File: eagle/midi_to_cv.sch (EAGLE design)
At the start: 58 parts, among them IC1 TL084P, IC2 TL084P, U1 ATMEGA328P_PDIP

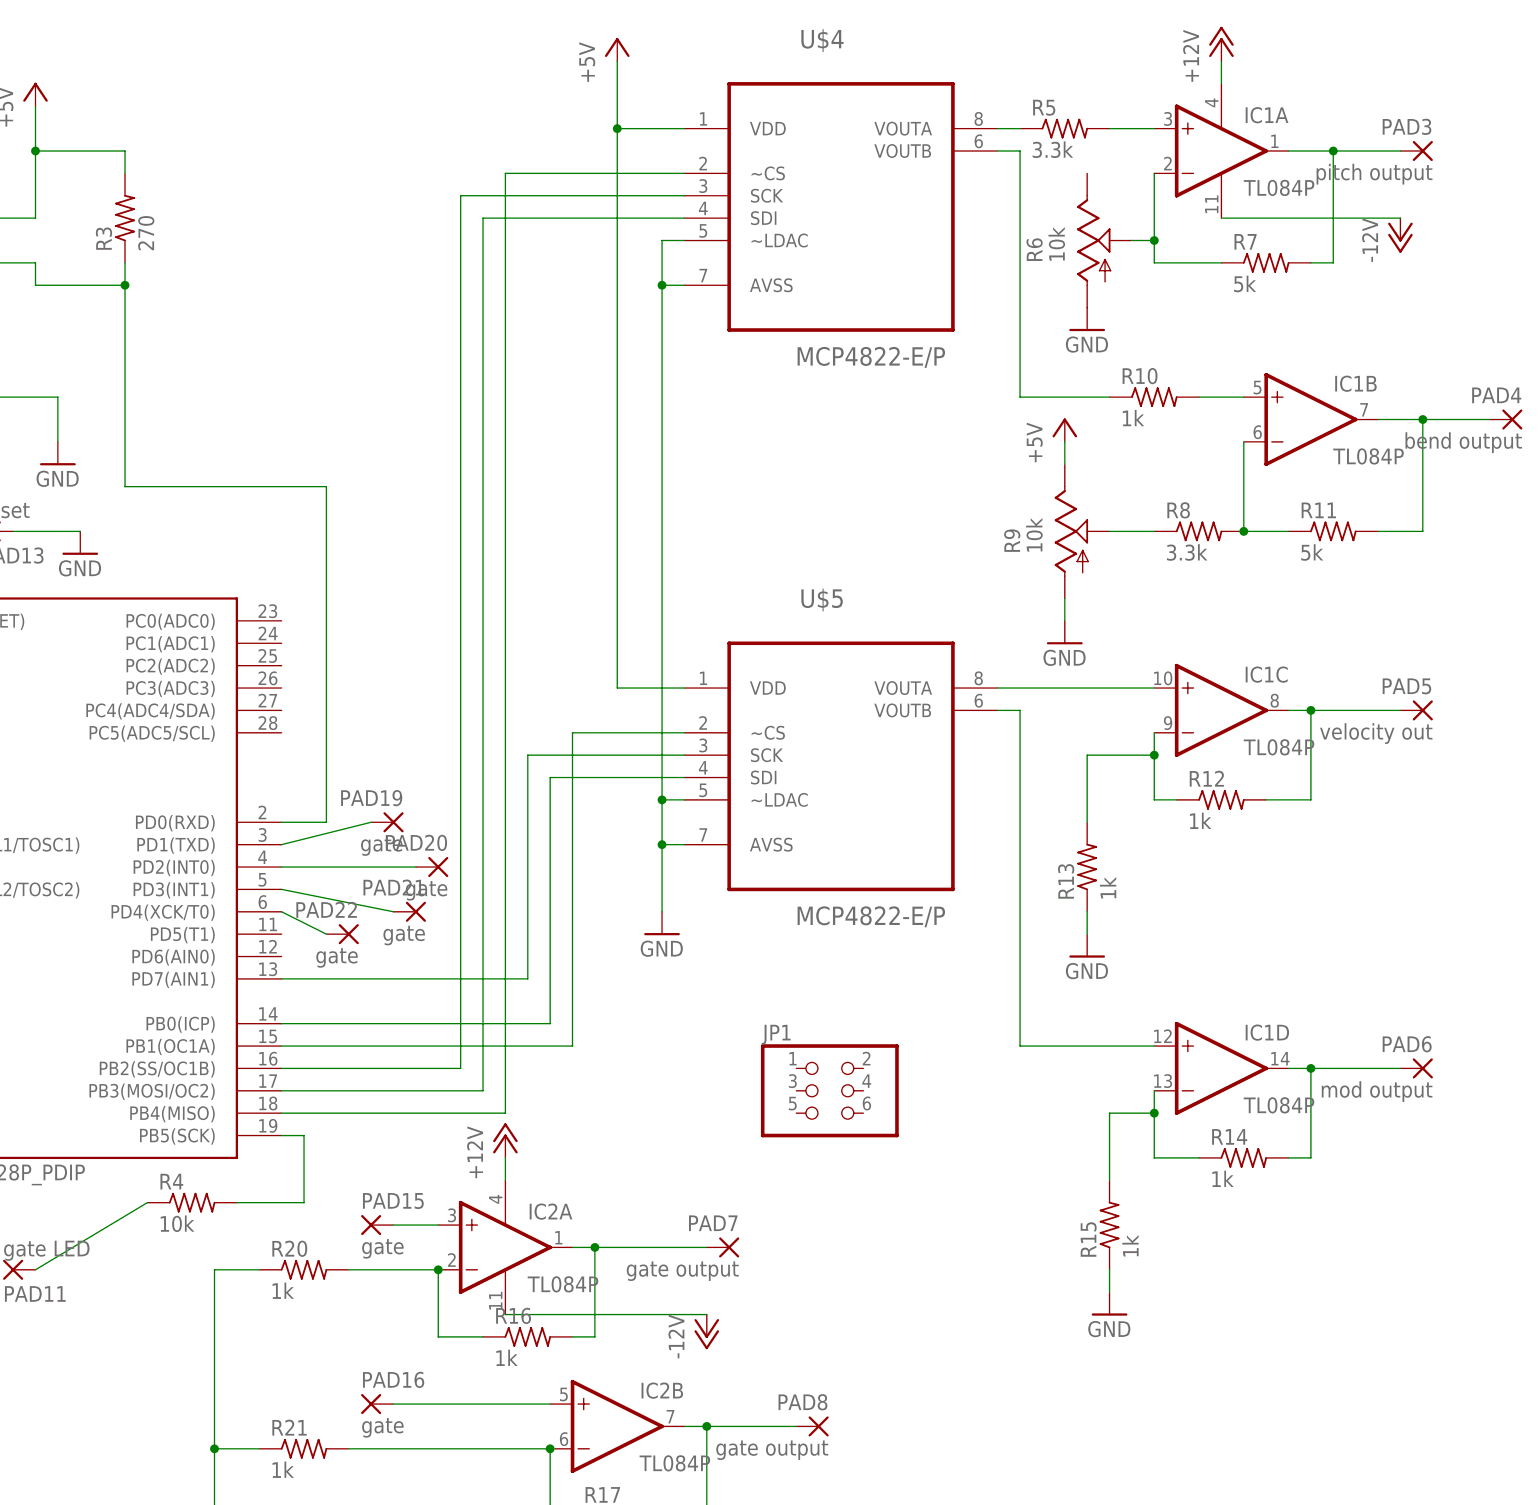
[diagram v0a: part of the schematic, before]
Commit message: converting to poly4
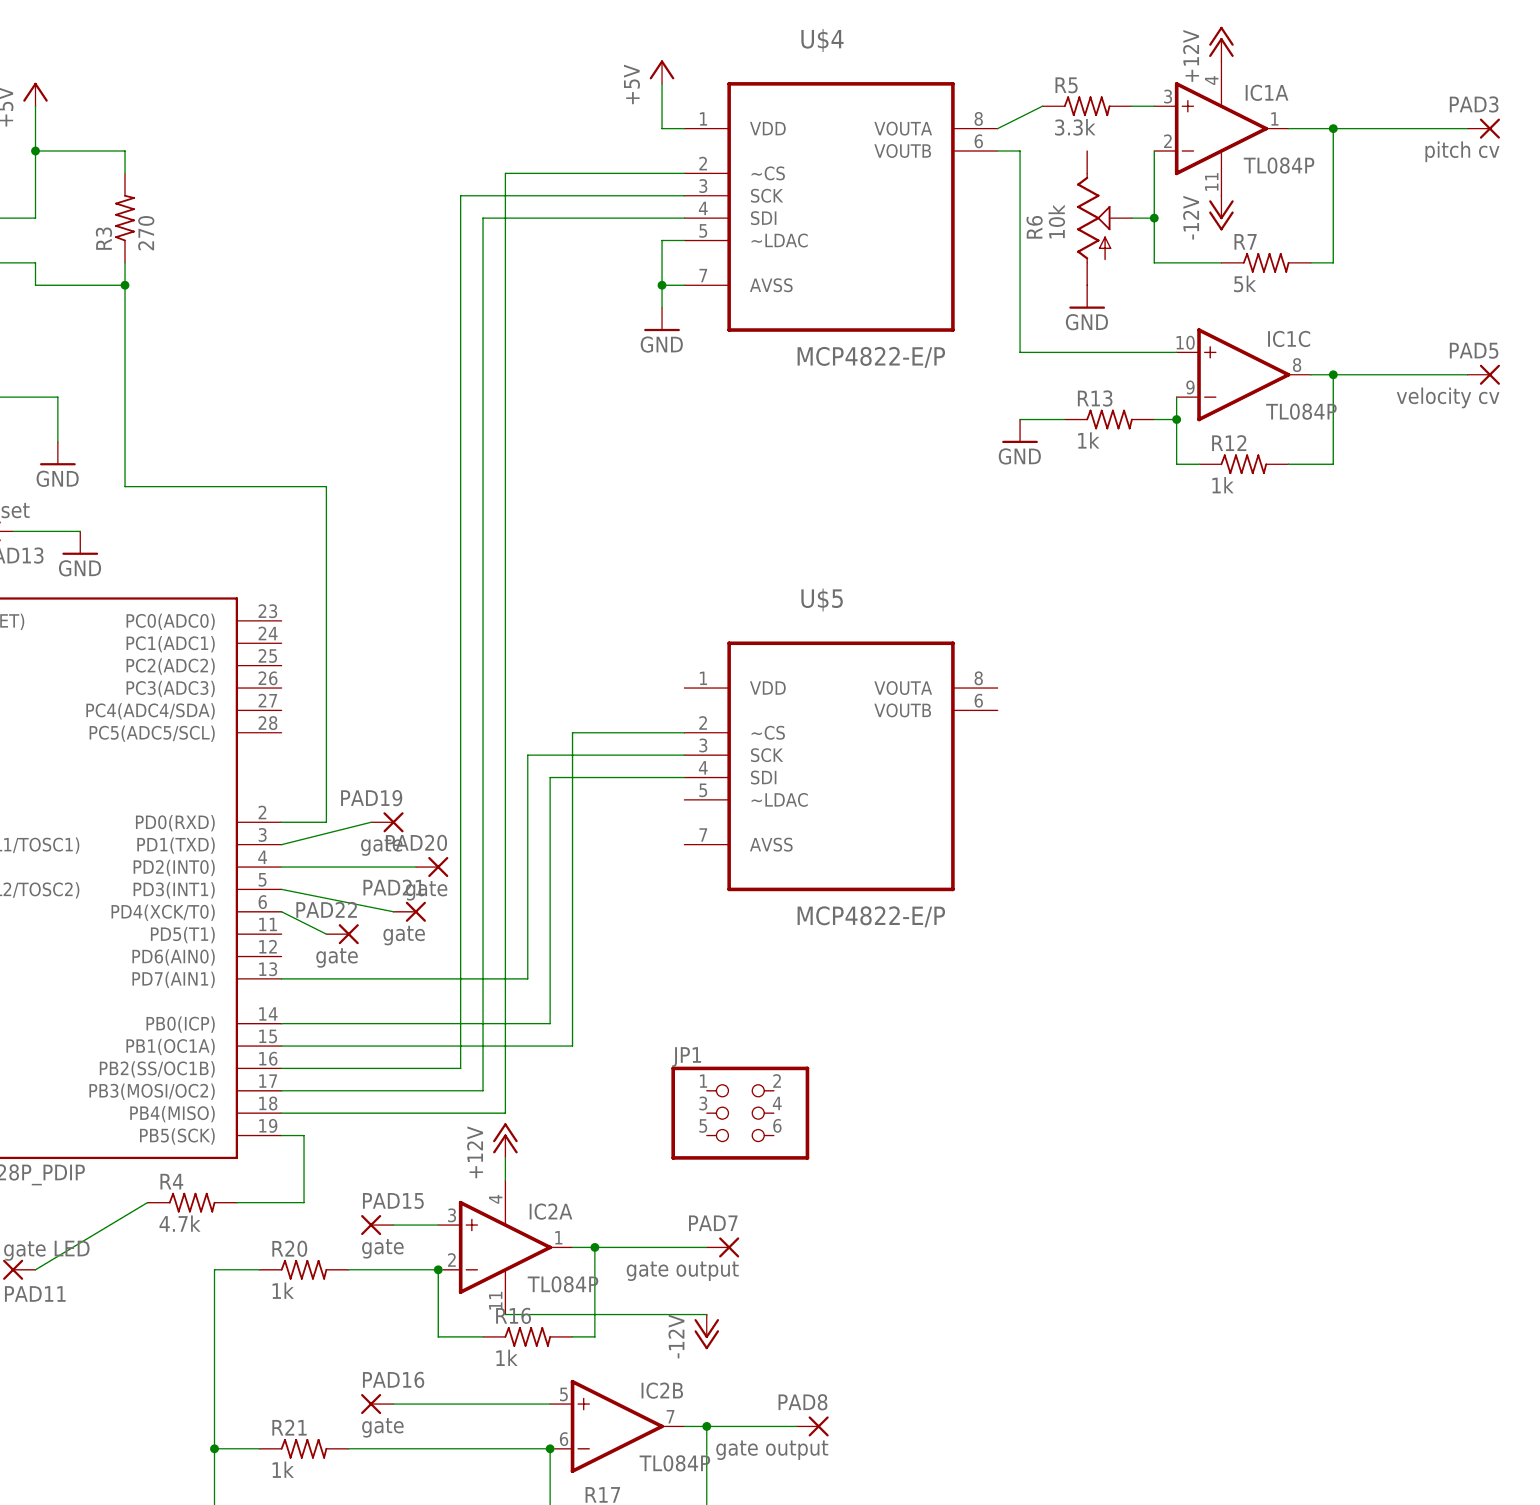
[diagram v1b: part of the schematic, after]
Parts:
- removed PAD4: bend output, wirepad:2,54/0,9
- removed PAD6: mod output, wirepad:2,54/0,9
- removed R10, R14, R15: 1k, rcl:R-US_0207/10
- removed R11: 5k, rcl:R-US_0207/10
- removed R8: 3.3k, rcl:R-US_0207/10
- removed R9: 10k, pot:TRIM_US-B64W
- PAD3: value pitch output -> pitch cv
- PAD5: value velocity out -> velocity cv
- R4: value 10k -> 4.7k
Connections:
- removed net N$13: IC1B.-IN, R11.1, R8.2
- removed net N$14: R10.1, U$4.VOUTB
- removed net N$15: IC1B.+IN, R10.2
- removed net N$16: R8.1, R9.S
- removed net N$17: IC1B.OUT, PAD4.P, R11.2
- removed net N$18: IC1C.+IN, U$5.VOUTA
- removed net N$21: IC1D.OUT, PAD6.P, R14.2
- removed net N$22: IC1D.-IN, R14.1, R15.2
- removed net N$24: IC1D.+IN, U$5.VOUTB
- new net N$51: IC1C.+IN, U$4.VOUTB
- net +5V: no longer R9.E, U$5.VDD
- net GND: no longer R15.1, R9.A, U$5.AVSS, U$5.~LDAC
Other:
- moved on the sheet: IC1A, IC1C, JP1, PAD3, PAD5, R12, R13, R5, R6

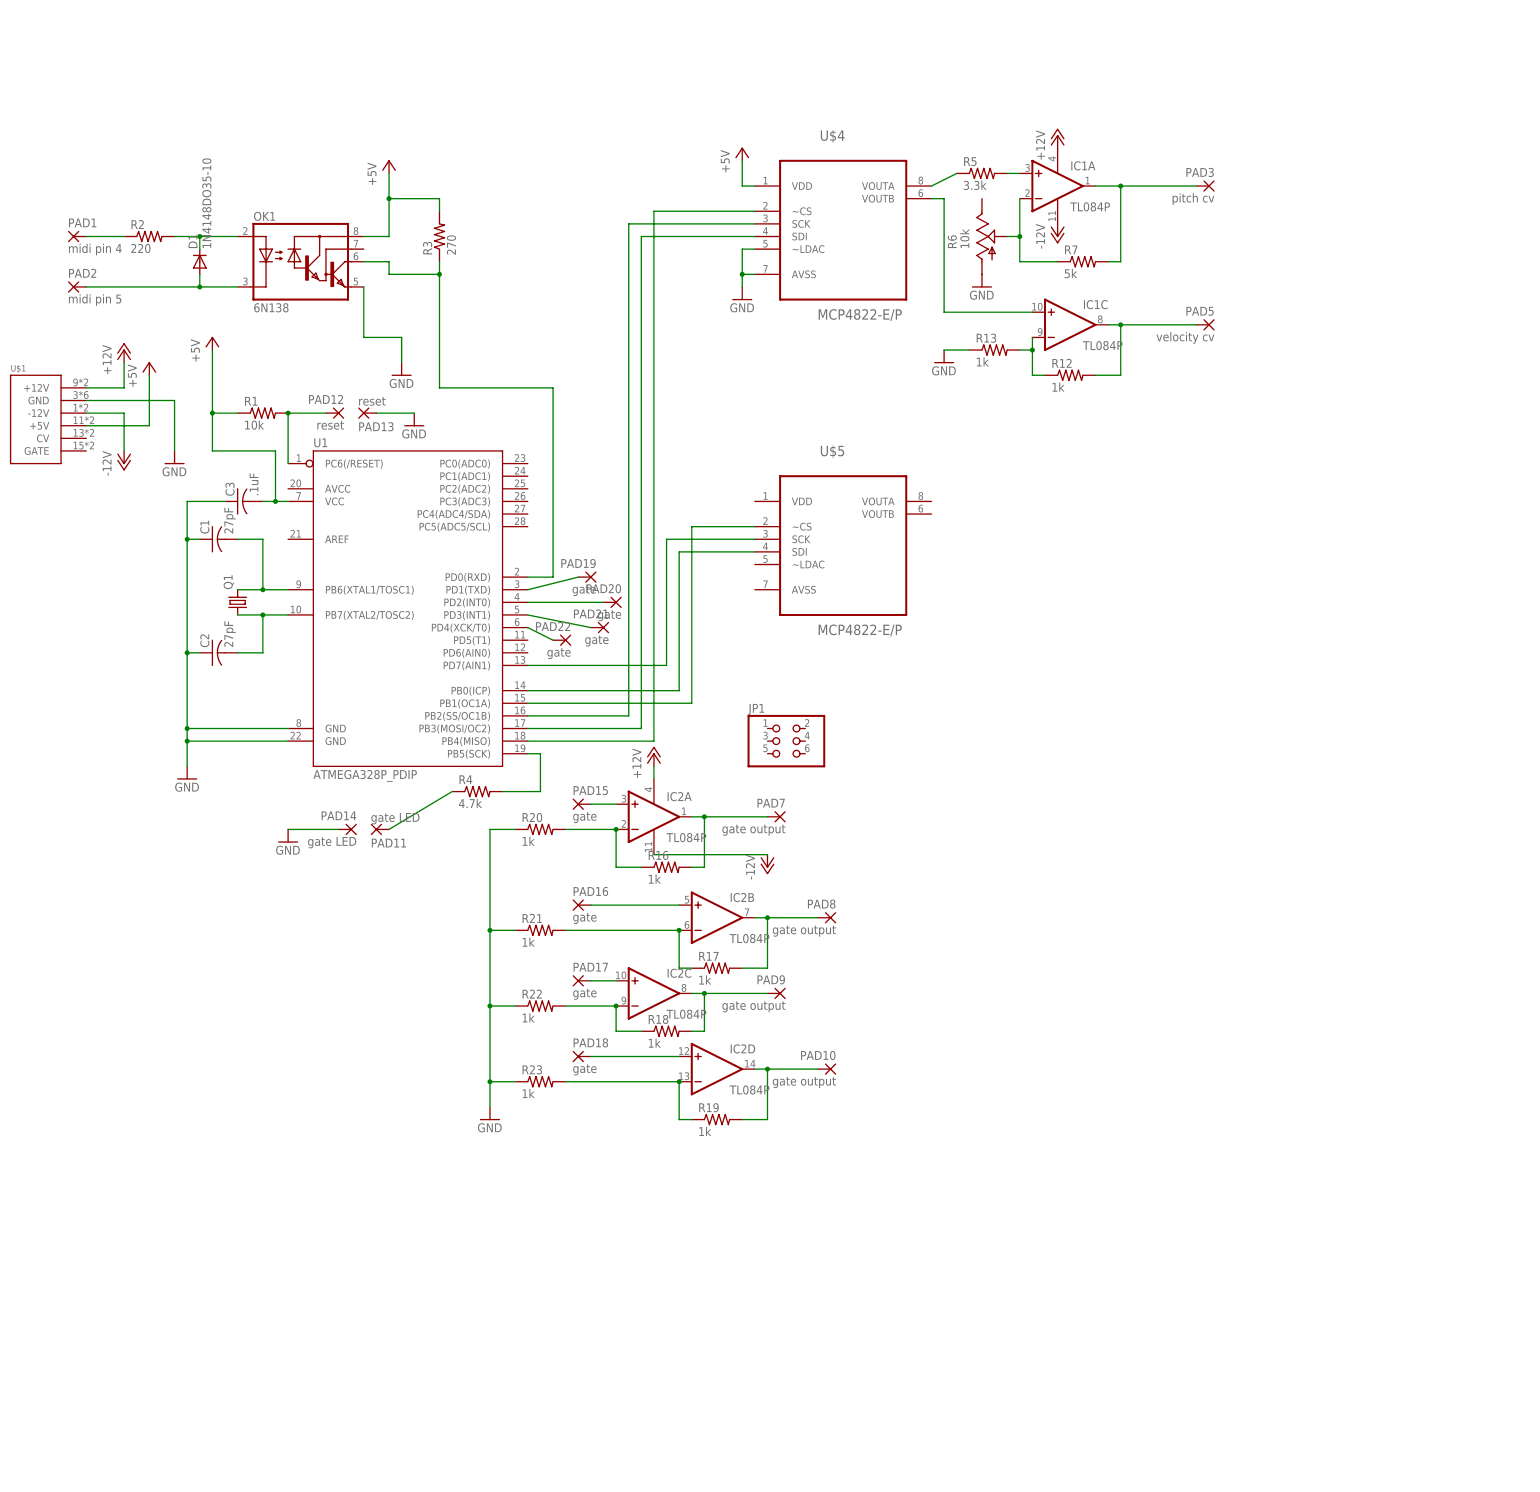
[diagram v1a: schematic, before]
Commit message: replicated pitch and velocity outputs four times
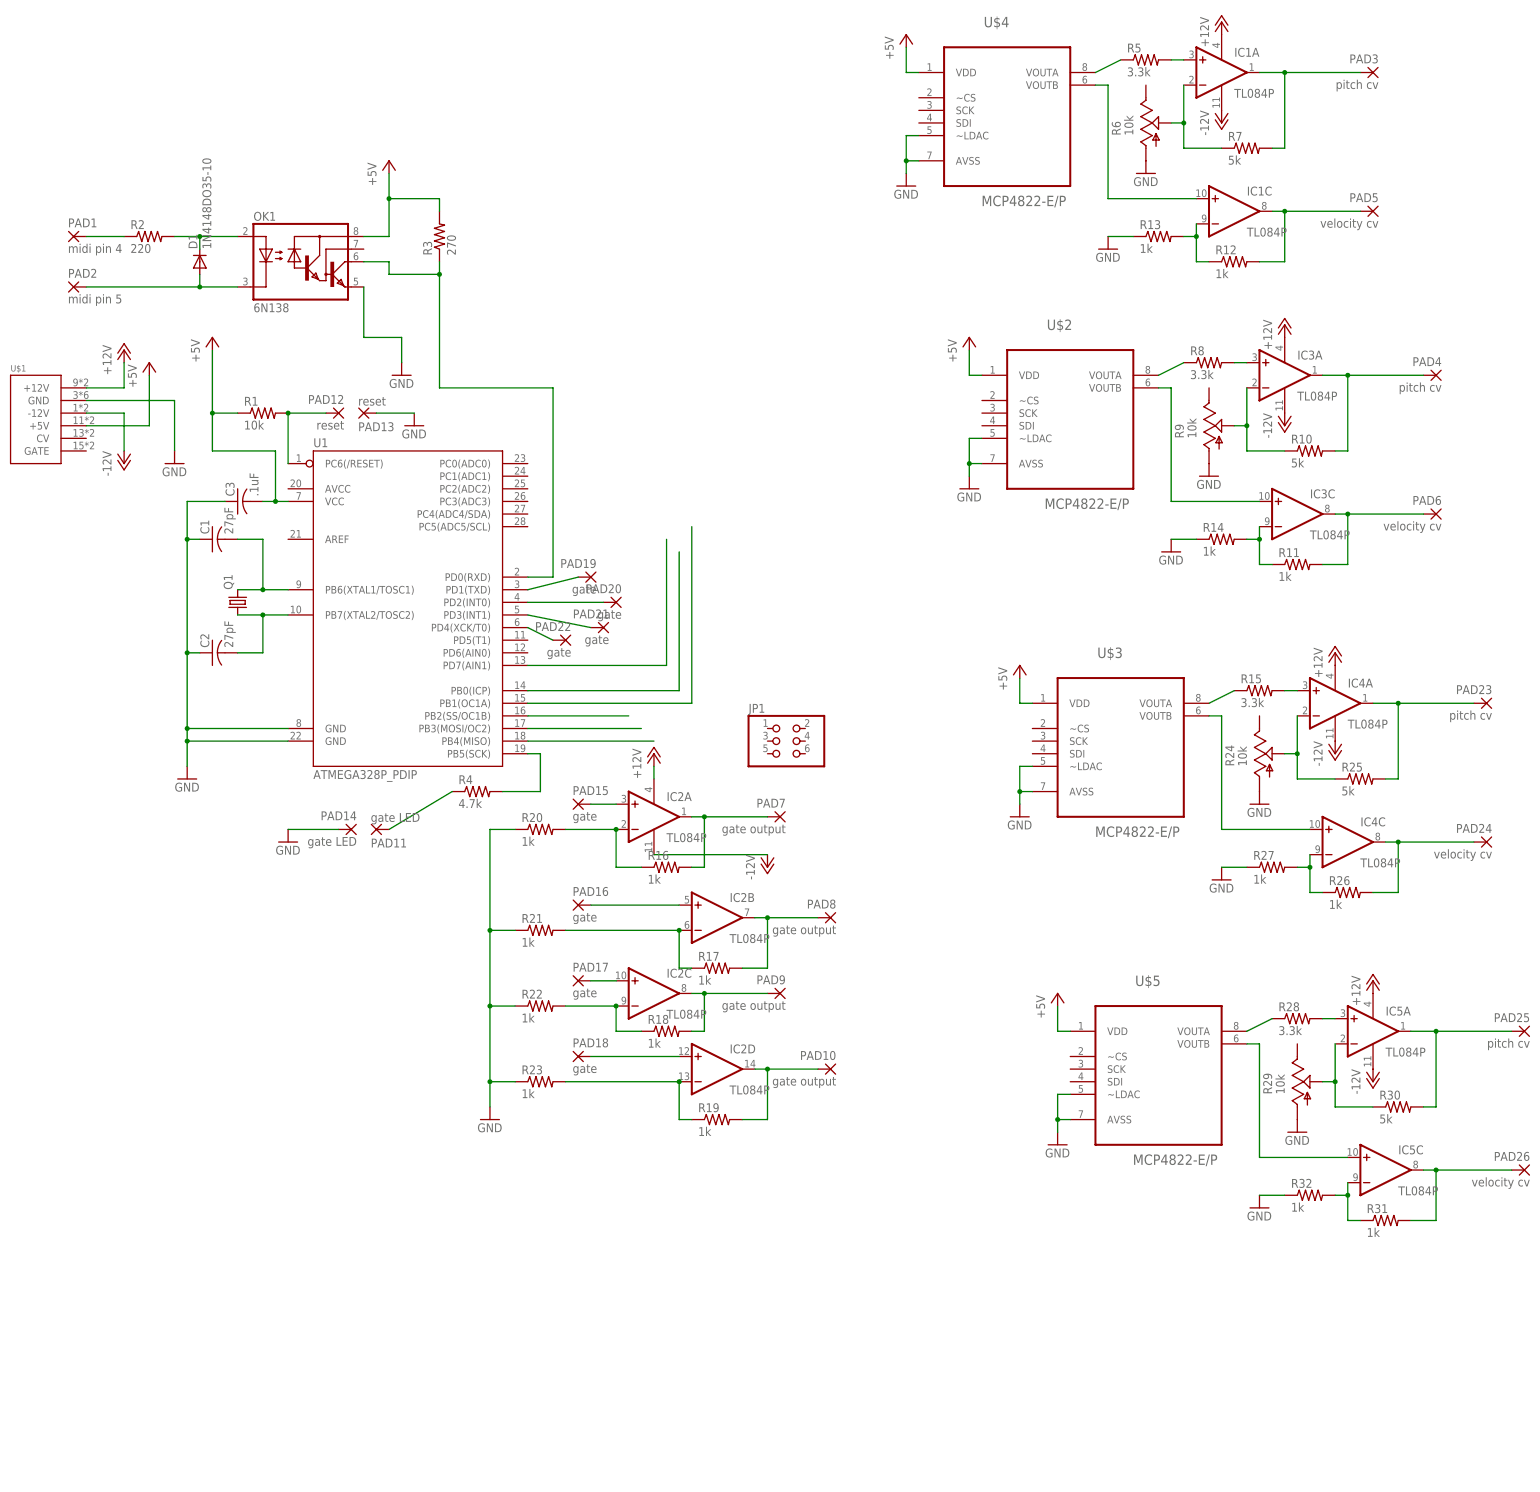
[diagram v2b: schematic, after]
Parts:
- added IC3, IC4, IC5: TL084P, linear:TL084P
- added PAD23, PAD25, PAD4: pitch cv, wirepad:2,54/0,9
- added PAD24, PAD26, PAD6: velocity cv, wirepad:2,54/0,9
- added R10, R25, R30: 5k, rcl:R-US_0207/10
- added R11, R14, R26, R27, R31, R32: 1k, rcl:R-US_0207/10
- added R15, R28, R8: 3.3k, rcl:R-US_0207/10
- added R24, R29, R9: 10k, pot:TRIM_US-B64W
- added U$2, U$3: MCP4822-E/P, MCP4822:MCP4822-E/P
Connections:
- new net N$13: R8.1, U$2.VOUTA
- new net N$14: U1.PB3(MOSI/OC2)
- new net N$15: U1.PB2(SS/OC1B)
- new net N$16: IC3A.+IN, R8.2
- new net N$17: IC3A.OUT, PAD4.P, R10.2
- new net N$18: IC3A.-IN, R10.1, R9.S
- new net N$21: IC3C.OUT, PAD6.P, R11.2
- new net N$22: IC3C.-IN, R11.1, R14.2
- new net N$24: IC3C.+IN, U$2.VOUTB
- new net N$49: IC4A.OUT, PAD23.P, R25.2
- new net N$50: IC4A.-IN, R24.S, R25.1
- new net N$52: IC4C.OUT, PAD24.P, R26.2
- new net N$53: IC4C.-IN, R26.1, R27.2
- new net N$54: IC4C.+IN, U$3.VOUTB
- new net N$55: R28.1, U$5.VOUTA
- new net N$56: IC5A.+IN, R28.2
- new net N$57: IC5A.OUT, PAD25.P, R30.2
- new net N$58: IC5A.-IN, R29.S, R30.1
- new net N$59: IC5C.OUT, PAD26.P, R31.2
- new net N$60: IC5C.-IN, R31.1, R32.2
- new net N$61: IC5C.+IN, U$5.VOUTB
- net +12V: now also IC3P.V+, IC4P.V+, IC5P.V+
- net +5V: now also U$2.VDD, U$3.VDD, U$5.VDD
- net -12V: now also IC3P.V-, IC4P.V-, IC5P.V-
- net GND: now also R14.1, R24.A, R27.1, R29.A, R32.1, R9.A, U$2.AVSS, U$2.~LDAC, U$3.AVSS, U$3.~LDAC, U$5.AVSS, U$5.~LDAC
- net N$23: no longer U$5.SDI
- net N$25: now also R15.1, U$3.VOUTA; no longer U$4.SCK, U1.PB2(SS/OC1B)
- net N$26: now also IC4A.+IN, R15.2; no longer U$4.SDI, U1.PB3(MOSI/OC2)
- net N$27: no longer U$4.~CS
- net N$28: no longer U$5.SCK
- net N$29: no longer U$5.~CS
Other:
- moved on the sheet: IC1A, IC1C, PAD3, PAD5, R12, R13, R5, R6, R7, U$4, U$5
